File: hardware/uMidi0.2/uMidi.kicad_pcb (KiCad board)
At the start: 2 copper layers, 71.1 x 43.2 mm, 43 parts, among them CON1 USB-MINI-B, IC1 6N138, IC2 ATXMEGA128A4U-M, P1 MIDI In, P2 MIDI Thru, P3 MIDI T/O, P4 MIDI Out, P5 5..12 V, P6 PDI, P7 GPIO1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

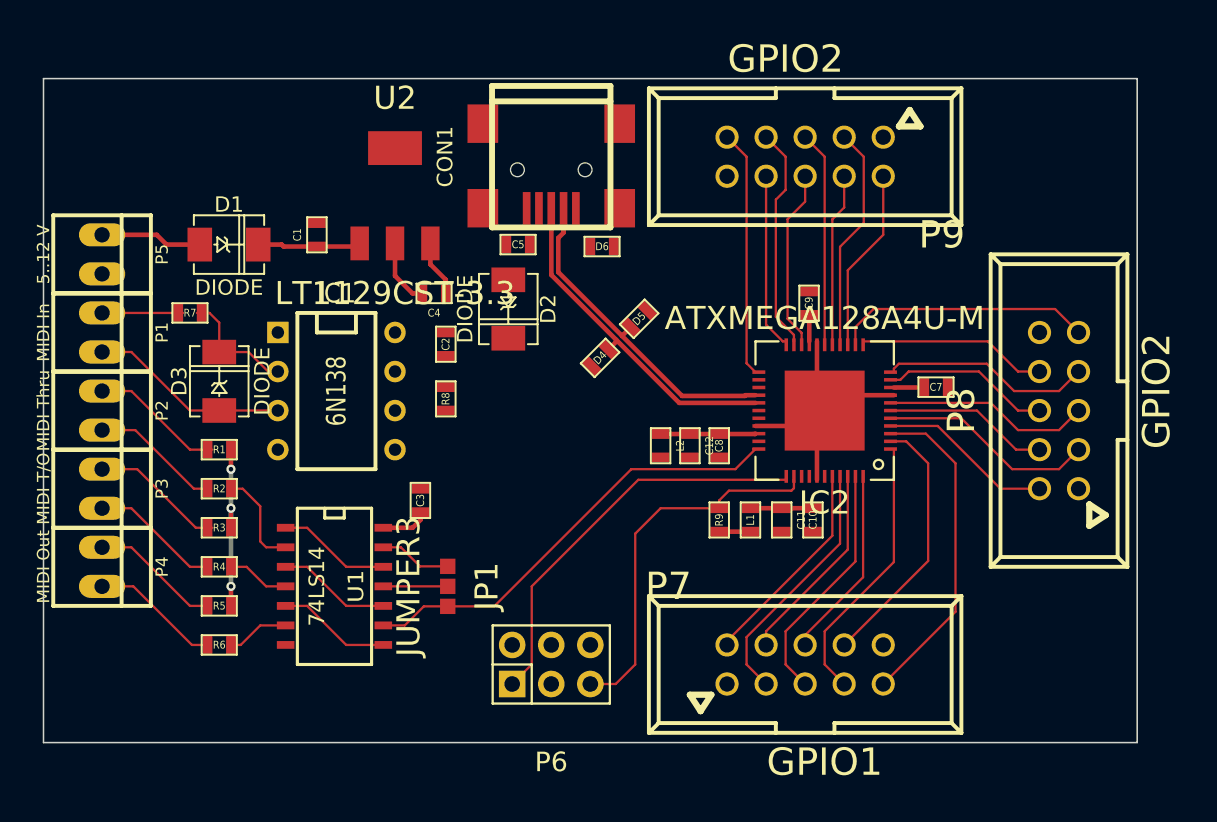
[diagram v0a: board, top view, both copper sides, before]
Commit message: Add ground plane
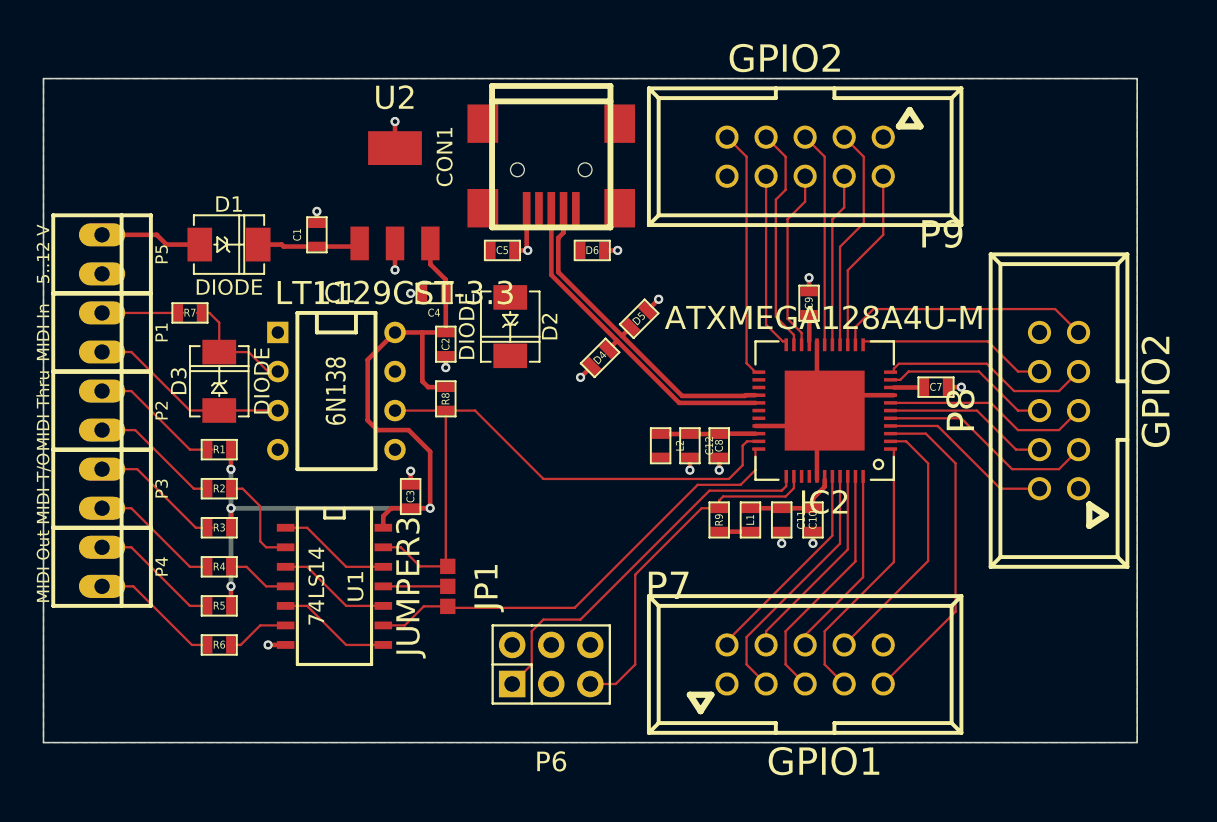
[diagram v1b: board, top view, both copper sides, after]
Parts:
- moved D2 1.15 mm to (97.7, 138.0)
- moved C5 1.09 mm to (97.2, 133.1)
- moved D6 0.68 mm to (103.0, 133.1)
- moved C3 0.68 mm to (91.2, 149.1)
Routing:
- net VCC: track 18.2 -> 57.8 mm, vias 3 -> 4
- net RXD: track 4.70 -> 41.9 mm
- net GND: track 23.6 -> 38.5 mm, vias 0 -> 17
- net Net-(C10-Pad1): track 4.06 -> 6.23 mm
- net Net-(IC2-Pad35): track 24.3 -> 22.8 mm
- net Net-(IC2-Pad34): track 26.3 -> 24.8 mm
- net TXD: track 29.1 -> 30.0 mm
- added copper zone on B.Cu, net GND

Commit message: Optimize placement; Reroute
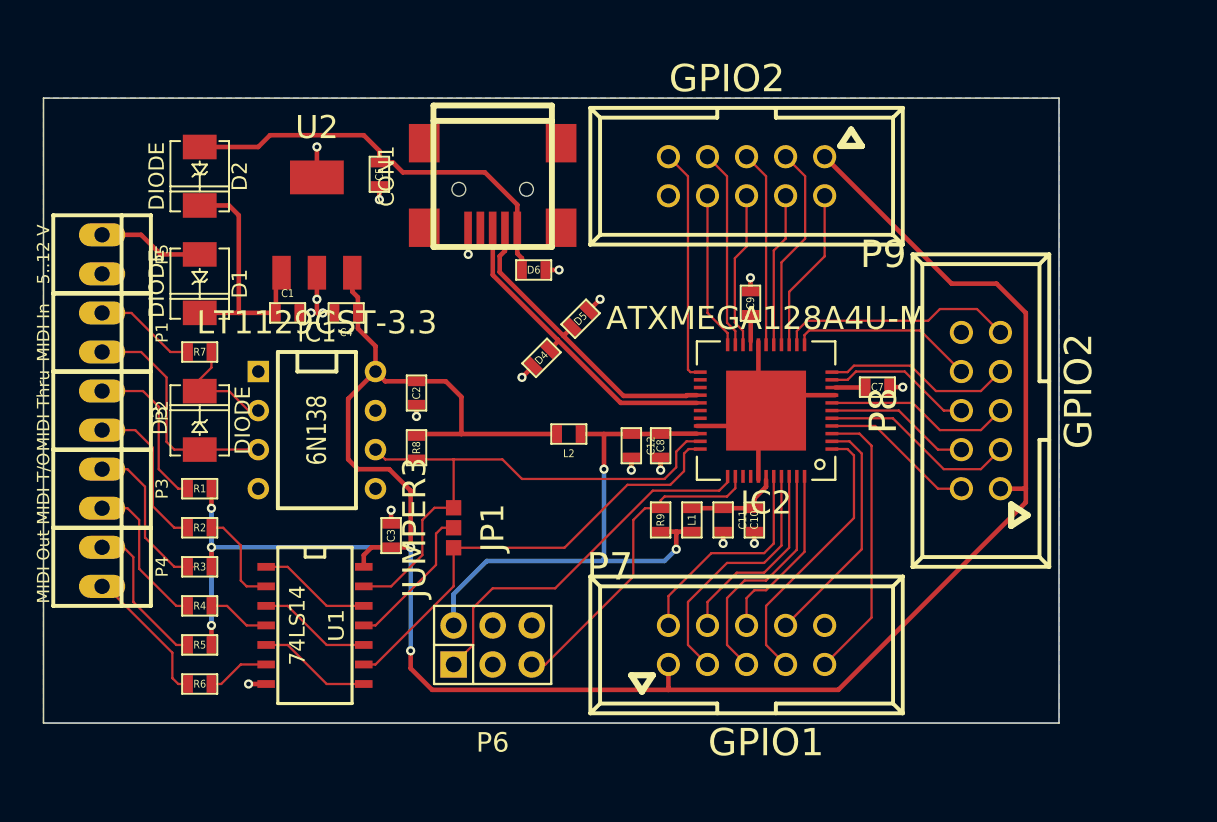
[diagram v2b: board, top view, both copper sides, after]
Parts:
- moved D2 22.4 mm to (77.5, 128.3)
- moved C5 9.41 mm to (89.2, 128.1), turned to 270 degrees
- moved L2 6.02 mm to (101.5, 145.0), turned to 0 degrees
- moved C4 5.85 mm to (87.0, 137.2)
- moved U2 5.43 mm to (85.1, 131.4)
- moved C1 5.43 mm to (83.2, 137.2), turned to 0 degrees
- moved P8 5.08 mm to (128.3, 143.5)
- moved CON1 4.02 mm to (96.5, 128.3)
- moved D6 4.02 mm to (99.2, 134.4)
- moved P6 4.02 mm to (96.5, 158.8)
- moved P7 4.02 mm to (113.0, 158.8)
- moved P9 4.02 mm to (113.0, 128.3)
- moved JP1 3.83 mm to (94.0, 151.1)
- moved C10 3.81 mm to (113.5, 150.6)
- moved C11 3.81 mm to (111.5, 150.6)
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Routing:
- net VCC: track 57.8 -> 155.3 mm, vias 4 -> 5
- net Net-(C12-Pad1): track 11.9 -> 40.9 mm, vias 0 -> 2
- net VBUS: track 0.00 -> 27.7 mm
- net Net-(C1-Pad1): track 6.73 -> 17.2 mm
- net RXD: track 41.9 -> 35.7 mm
- net Net-(JP1-Pad2): track 4.19 -> 9.66 mm
- net Net-(IC2-Pad3): track 21.1 -> 18.2 mm
- net Net-(D3-Pad1): track 13.0 -> 15.2 mm
- net Net-(P2-Pad2): track 8.44 -> 10.5 mm
- net Net-(P2-Pad1): track 8.75 -> 10.6 mm
- net Net-(IC2-Pad21): track 14.6 -> 12.8 mm
- net Net-(IC2-Pad35): track 22.8 -> 21.0 mm
- net Net-(P3-Pad1): track 8.62 -> 10.3 mm
- net Net-(P3-Pad2): track 8.44 -> 10.1 mm
- net Net-(IC2-Pad2): track 16.9 -> 15.3 mm
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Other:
- board size 71.1 x 43.2 mm -> 66 x 40.6 mm

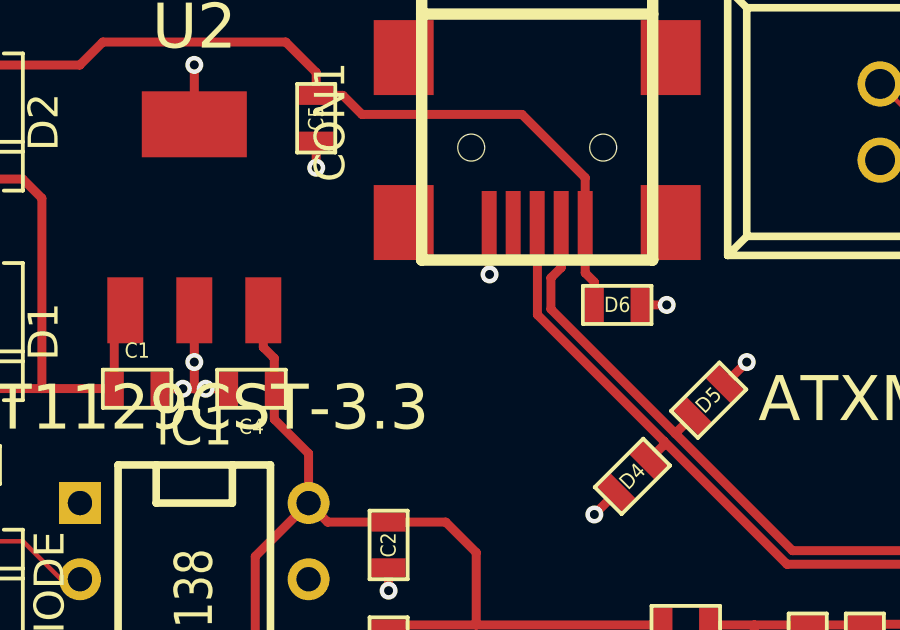
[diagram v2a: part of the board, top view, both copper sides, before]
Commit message: Add filter network between USB shield and GND
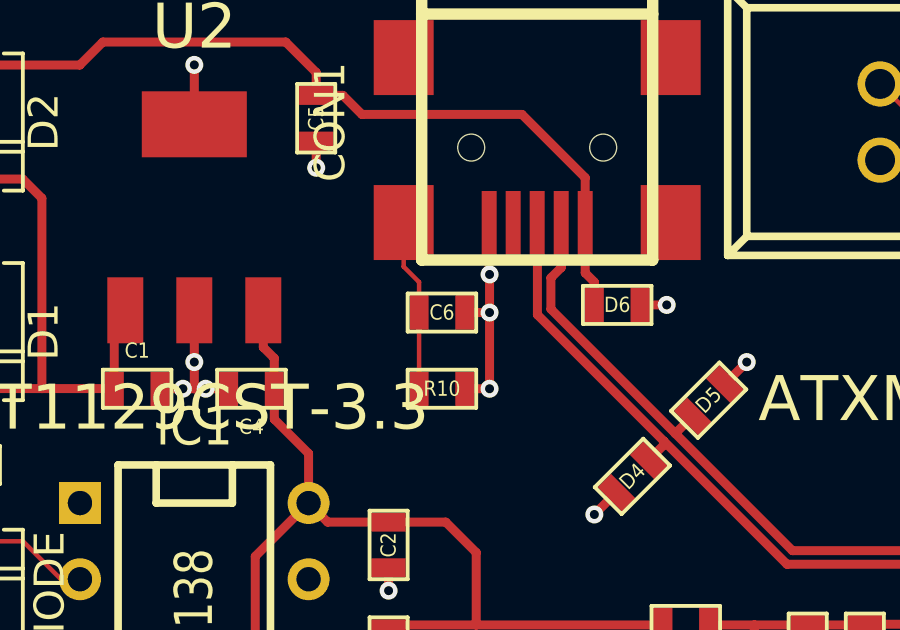
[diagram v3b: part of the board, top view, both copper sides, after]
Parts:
- added C6: 4.7n, SMD_Packages:SMD-0603, F.Cu at (93.3, 134.6)
- added R10: 1M, SMD_Packages:SMD-0603, F.Cu at (93.3, 137.2)
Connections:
- net VCC renamed +3.3V
- CON1 pad 7: Net-(CON1-Pad6) -> Net-(CON1-Pad7)
- CON1 pad 8: Net-(CON1-Pad6) -> Net-(C6-Pad2)
- CON1 pad 9: Net-(CON1-Pad6) -> Net-(CON1-Pad9)
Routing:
- net Net-(C6-Pad2): track 0.00 -> 5.75 mm
- net GND: track 39.4 -> 44.8 mm, vias 18 -> 20

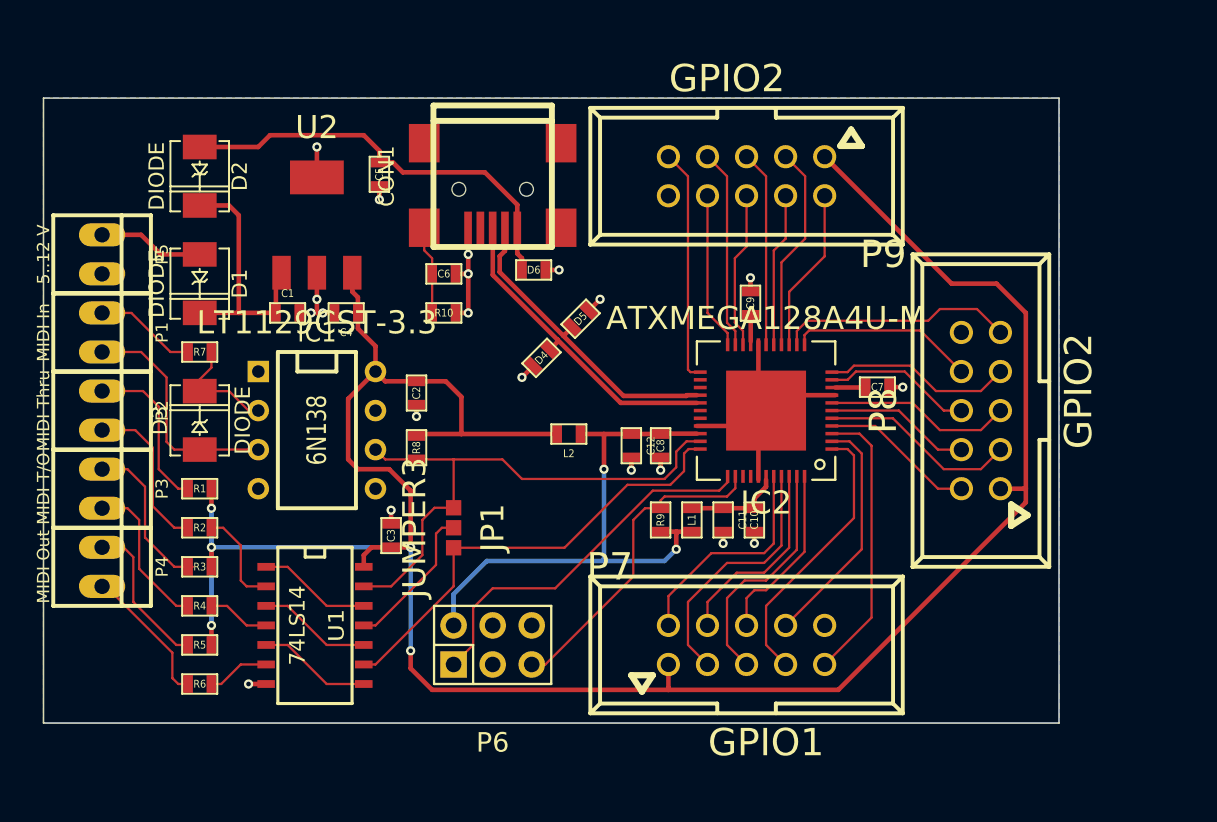
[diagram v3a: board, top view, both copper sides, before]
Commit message: Add mounting holes
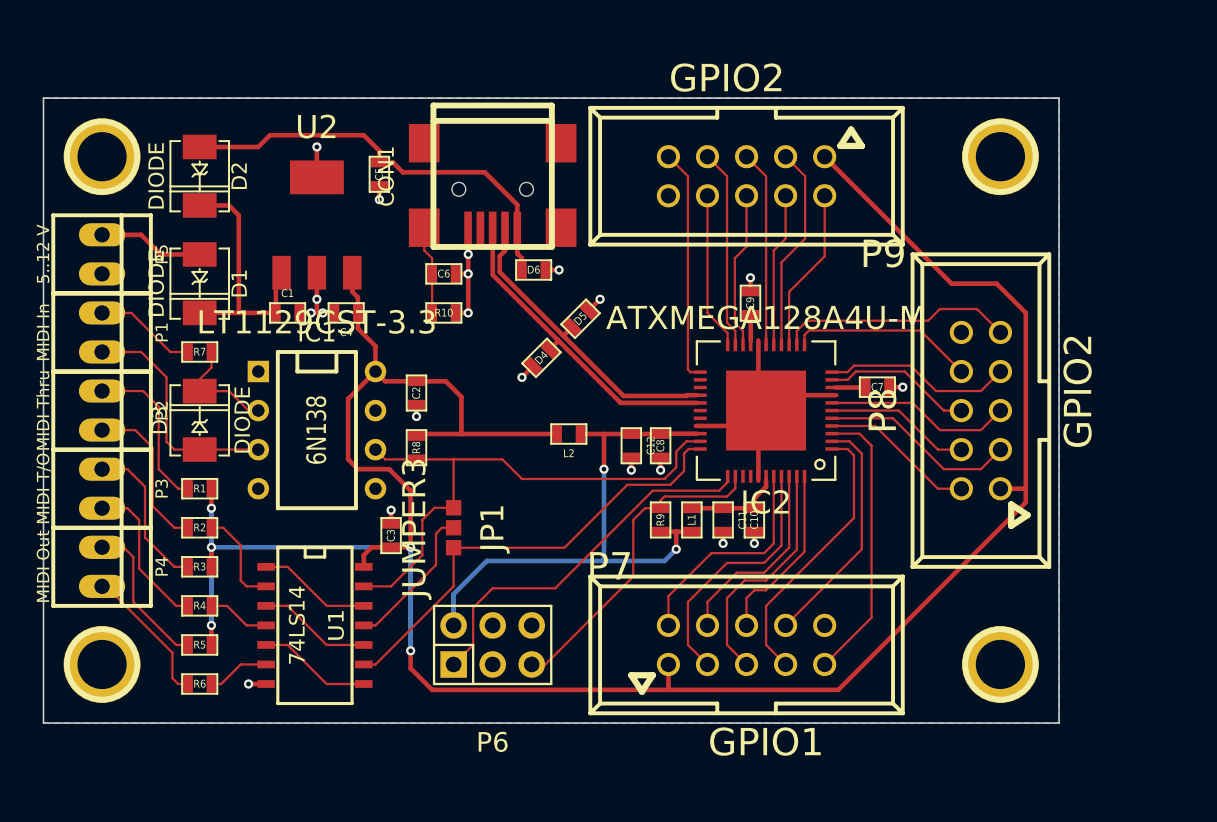
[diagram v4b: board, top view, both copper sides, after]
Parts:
- added 1PIN: P***, Connect:1pin, F.Cu at (71.1, 127.0)
- added 1PIN: P***, Connect:1pin, F.Cu at (71.1, 160.0)
- added 1PIN: P***, Connect:1pin, F.Cu at (129.5, 160.0)
- added 1PIN: P***, Connect:1pin, F.Cu at (129.5, 127.0)
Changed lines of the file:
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@@
 (kicad_pcb (version 4) (host pcbnew "(2014-09-08 BZR 5122)-product")
   (general
-    (links 121)
+    (links 125)
     (no_connects 4)
     (area 67.259999 123.139999 133.400001 163.880001)
@@
     (tracks 408)
     (zones 0)
-    (modules 45)
+    (modules 49)
     (nets 68)
   )
@@
     (mod_text_size 1 1)
     (mod_text_width 0.15)
-    (pad_size 1.5 1.5)
-    (pad_drill 0.6)
+    (pad_size 5 5)
+    (pad_drill 3.2)
     (pad_to_mask_clearance 0)
     (aux_axis_origin 0 0)
-    (visible_elements FFFFFF1F)
+    (visible_elements FFFFFF7F)
     (pcbplotparams
       (layerselection 0x00030_80000001)
@@
     )
   )
+  (module Connect:1pin (layer F.Cu)
+    (at 71.12 127)
+    (descr "module 1 pin (ou trou mecanique de percage)")
+    (tags DEV)
+    (fp_text reference 1PIN (at 0 -3.048) (layer F.SilkS) hide
+      (effects (font (size 1.016 1.016) (thickness 0.254)))
+    )
+    (fp_text value P*** (at 0 2.794) (layer F.SilkS) hide
+      (effects (font (size 1.016 1.016) (thickness 0.254)))
+    )
+    (fp_circle (center 0 0) (end 0 -2.286) (layer F.SilkS) (width 0.381))
+    (pad 1 thru_hole circle (at 0 0) (size 5 5) (drill 3.2) (layers *.Cu *.Mask F.SilkS)
+      (net 2 GND))
+  )
+  (module Connect:1pin (layer F.Cu)
+    (at 71.12 160.02)
+    (descr "module 1 pin (ou trou mecanique de percage)")
+    (tags DEV)
+    (fp_text reference 1PIN (at 0 -3.048) (layer F.SilkS) hide
+      (effects (font (size 1.016 1.016) (thickness 0.254)))
+    )
+    (fp_text value P*** (at 0 2.794) (layer F.SilkS) hide
+      (effects (font (size 1.016 1.016) (thickness 0.254)))
+    )
+    (fp_circle (center 0 0) (end 0 -2.286) (layer F.SilkS) (width 0.381))
+    (pad 1 thru_hole circle (at 0 0) (size 5 5) (drill 3.2) (layers *.Cu *.Mask F.SilkS)
+      (net 2 GND))
+  )
+  (module Connect:1pin (layer F.Cu)
+    (at 129.54 160.02)
+    (descr "module 1 pin (ou trou mecanique de percage)")
+    (tags DEV)
+    (fp_text reference 1PIN (at 0 -3.048) (layer F.SilkS) hide
+      (effects (font (size 1.016 1.016) (thickness 0.254)))
+    )
+    (fp_text value P*** (at 0 2.794) (layer F.SilkS) hide
+      (effects (font (size 1.016 1.016) (thickness 0.254)))
+    )
+    (fp_circle (center 0 0) (end 0 -2.286) (layer F.SilkS) (width 0.381))
+    (pad 1 thru_hole circle (at 0 0) (size 5 5) (drill 3.2) (layers *.Cu *.Mask F.SilkS)
+      (net 2 GND))
+  )
+  (module Connect:1pin (layer F.Cu)
+    (at 129.54 127)
+    (descr "module 1 pin (ou trou mecanique de percage)")
+    (tags DEV)
+    (fp_text reference 1PIN (at 0 -3.048) (layer F.SilkS) hide
+      (effects (font (size 1.016 1.016) (thickness 0.254)))
+    )
+    (fp_text value P*** (at 0 2.794) (layer F.SilkS) hide
+      (effects (font (size 1.016 1.016) (thickness 0.254)))
+    )
+    (fp_circle (center 0 0) (end 0 -2.286) (layer F.SilkS) (width 0.381))
+    (pad 1 thru_hole circle (at 0 0) (size 5 5) (drill 3.2) (layers *.Cu *.Mask)
+      (net 2 GND))
+  )
   (gr_line (start 133.35 163.83) (end 67.31 163.83) (angle 90) (layer Edge.Cuts) (width 0.1))
   (gr_line (start 67.31 123.19) (end 133.35 123.19) (angle 90) (layer Edge.Cuts) (width 0.1))
@@
   (via (at 94.9325 134.62) (size 0.6) (layers F.Cu B.Cu) (net 2))
   (via (at 94.9325 137.16) (size 0.6) (layers F.Cu B.Cu) (net 2))
-  (segment (start 94.9325 137.16) (end 94.107 137.16) (width 0.3) (layer F.Cu) (net 2) (status 800000))
+  (segment (start 94.9325 137.16) (end 94.107 137.16) (width 0.3) (layer F.Cu) (net 2))
   (segment (start 94.9325 134.62) (end 94.9325 133.35) (width 0.3) (layer F.Cu) (net 2))
-  (segment (start 94.107 134.62) (end 94.9325 134.62) (width 0.3) (layer F.Cu) (net 2) (status 400000))
+  (segment (start 94.107 134.62) (end 94.9325 134.62) (width 0.3) (layer F.Cu) (net 2))
   (segment (start 85.09 137.16) (end 85.09 136.271) (width 0.3) (layer F.Cu) (net 2))
   (via (at 85.09 136.271) (size 0.6) (layers F.Cu B.Cu) (net 2))

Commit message: Add thermal vias below MCU
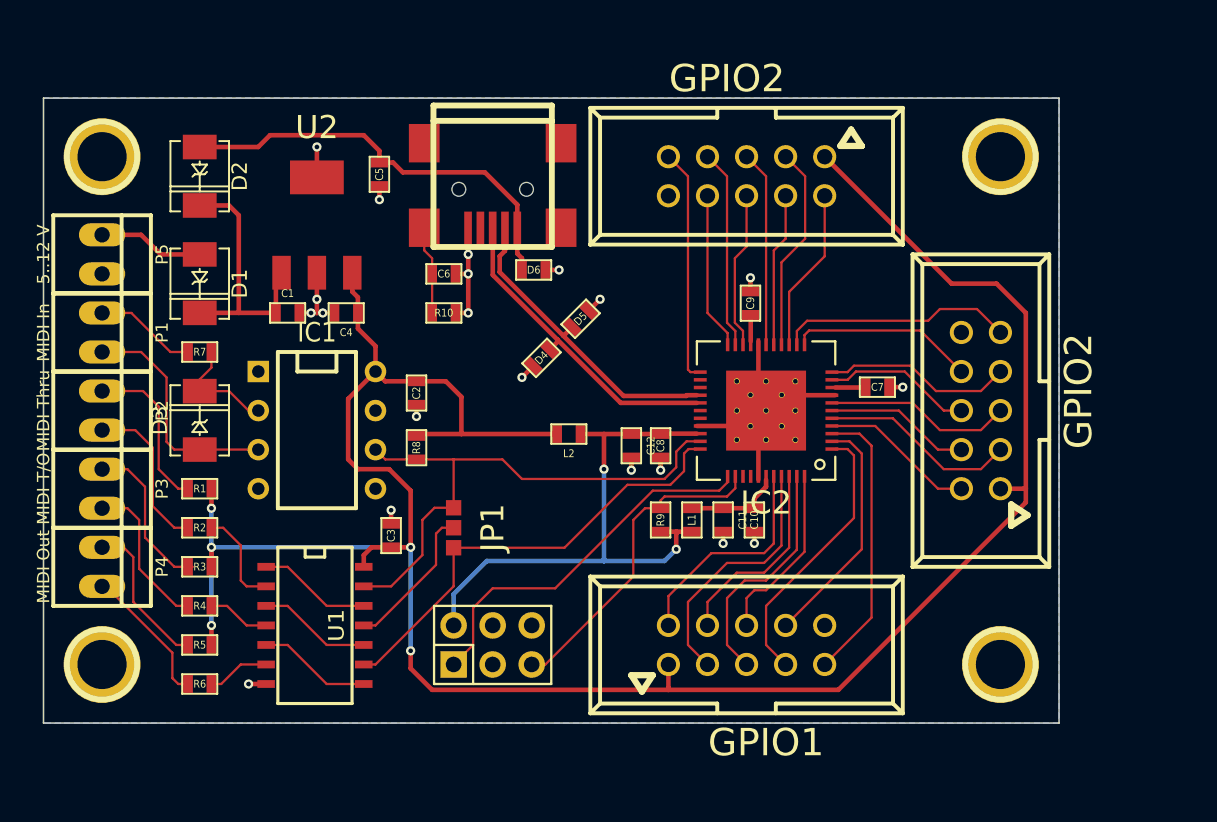
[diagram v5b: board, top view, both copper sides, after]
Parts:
- IC2: footprint SMD_Packages:QFN-44-1EP -> Atmel:QFN-44-1EP
